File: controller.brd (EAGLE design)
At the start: 46.3 x 36.8 mm, 27 parts, among them U1 10118194-MICRO-USB, U2 LM3671MF-3.3/NOPBMF05A-M, U3 SN74LVC1T45DBVRDBV6-M, U4 SN74LVC1T45DBVRDBV6-M, U5 SS8050-G, U6 SS8050-G

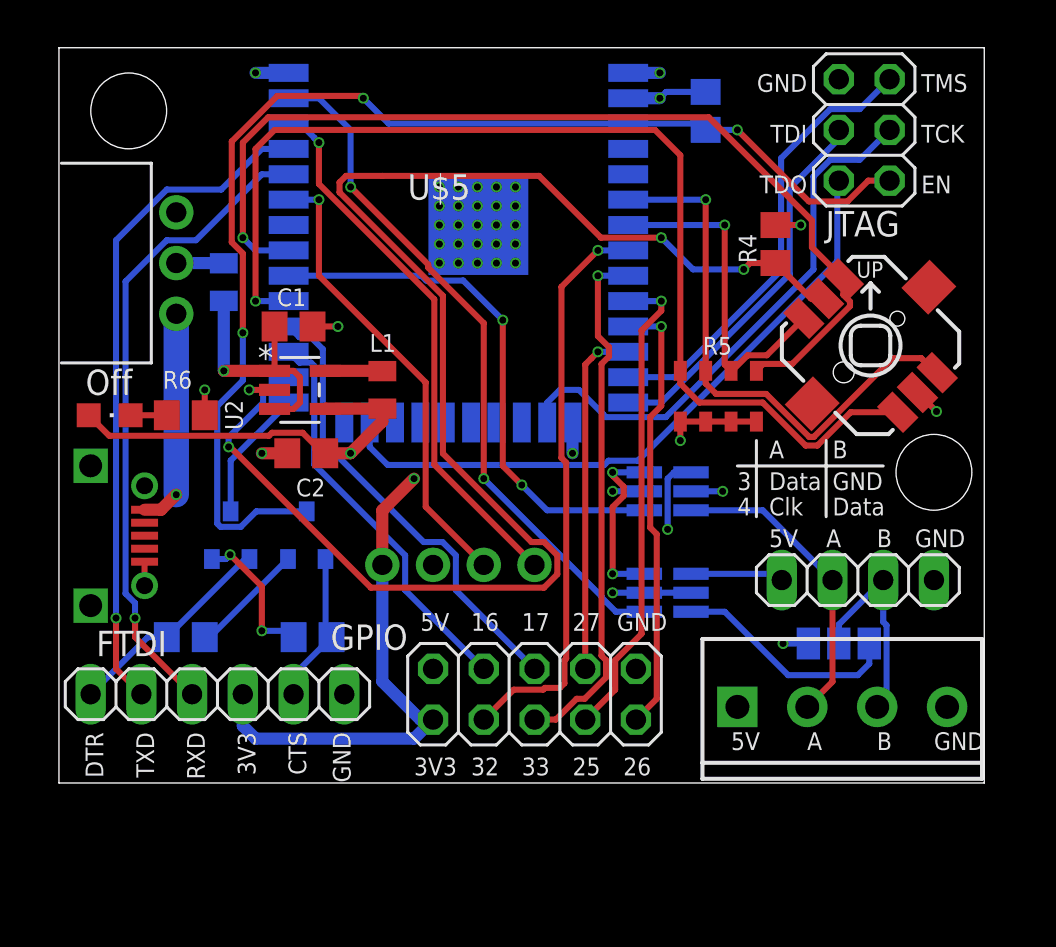
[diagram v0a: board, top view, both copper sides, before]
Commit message: Fixed a bunch of bugs in v1.0
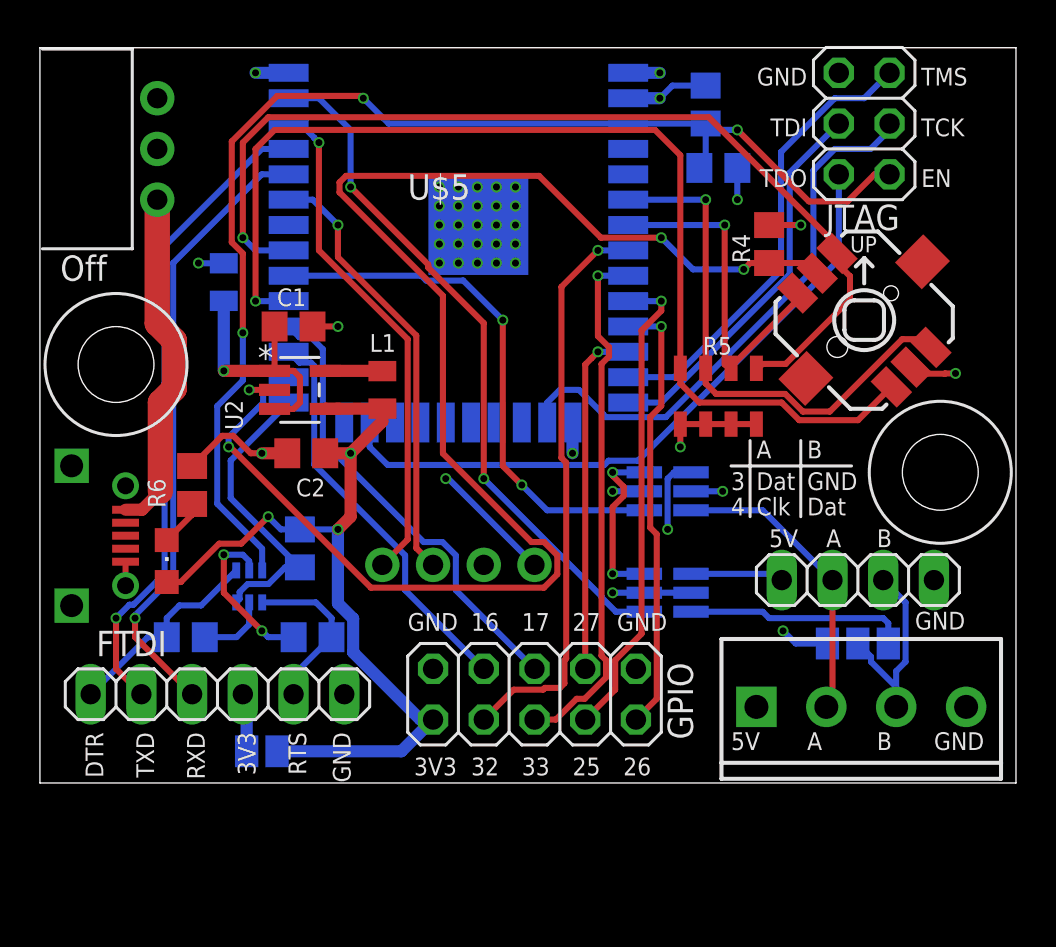
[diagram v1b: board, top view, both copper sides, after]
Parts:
- removed U6: SS8050-G, nebrius:SC-59
- added C3: 0.1uF, rcl:C0805
- added R7: (no value), rcl:R0805
- added SJ2: (no value), jumper:SJ
- R6: value 220 -> 1k
- U5: value SS8050-G -> MBT3904DW1T1; device nebrius:SC-59 -> nebrius:SOT363
- moved LED1 7.84 mm to (84.5, 56.8), turned to 0 degrees
- moved U$3 5.79 mm to (84.0, 77.5)
- moved U5 3.82 mm to (88.6, 55.6), turned to 0 degrees
- moved R6 3.51 mm to (85.7, 60.6), turned to 270 degrees
- moved S1 1.31 mm to (119.4, 68.9)
- moved J1 0.95 mm to (114.0, 49.5)
- moved SJ1 0.95 mm to (119.1, 52.7)
- moved U1 0.95 mm to (79.7, 58.1)
- moved JP3 0.32 mm to (119.4, 78.7)
- moved R3 0.32 mm to (111.4, 79.7)
- moved R4 0.32 mm to (114.6, 72.7)
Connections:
- new net N$11: JP2.3, SJ2.1
- net +5V: no longer JP7.2
- net EN: now also C3.1, U5.6; no longer U5.3
- net GND: now also C3.2, JP7.2, U$5.3; no longer U$5.2
- net IO0: now also R7.1, U5.3; no longer U6.3
- net N$12: now also JP2.2, R2.2, U5.1; no longer JP2.6, R1.2, U6.2
- net N$4: now also U5.2; no longer U5.1
- net N$5: now also U5.5; no longer U6.1
- net N$6: now also JP2.6, R1.2, U5.4; no longer JP2.2, R2.2, U5.2
- net SCL: now also U$5.2; no longer U$5.3
- net SDA: now also U$5.1; no longer U$5.4
- net VCC: now also R7.2, SJ2.2, U$5.4; no longer JP2.3, U$5.1
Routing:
- net IO0: track 6.65 -> 15.0 mm
- net GND: track 21.8 -> 28.8 mm
- net N$2: track 11.0 -> 17.4 mm, vias 1 -> 0
- net N$11: track 0.00 -> 2.94 mm
- net VCC: track 64.5 -> 67.4 mm, vias 7 -> 9
- net N$6: track 7.68 -> 10.4 mm
- net N$12: track 10.8 -> 8.40 mm
- net N$4: track 5.79 -> 3.59 mm
- net SDA: track 27.5 -> 25.4 mm
- net TXD: track 33.8 -> 32.3 mm
- net RXD: track 32.4 -> 31.2 mm
- net SCL: track 23.2 -> 22.0 mm
- net RIGHT: track 27.7 -> 26.6 mm
- net +5V: track 10.9 -> 9.81 mm, vias 1 -> 2
- net N$5: track 7.19 -> 8.19 mm
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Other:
- board size 46.3 x 36.8 mm -> 48.9 x 36.8 mm
- board text added: "Dat"
- board text added: "RTS"
- board text added: "RVL Controller v1.1 Copyright Bryan Hughes October 2019"
- board text removed: "CTS"
- board text removed: "Data"
- board text removed: "RVL Controller v1.0 Copyright Bryan Hughes October 2019"

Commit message: Tweaks and bug fixes from v1.1 board
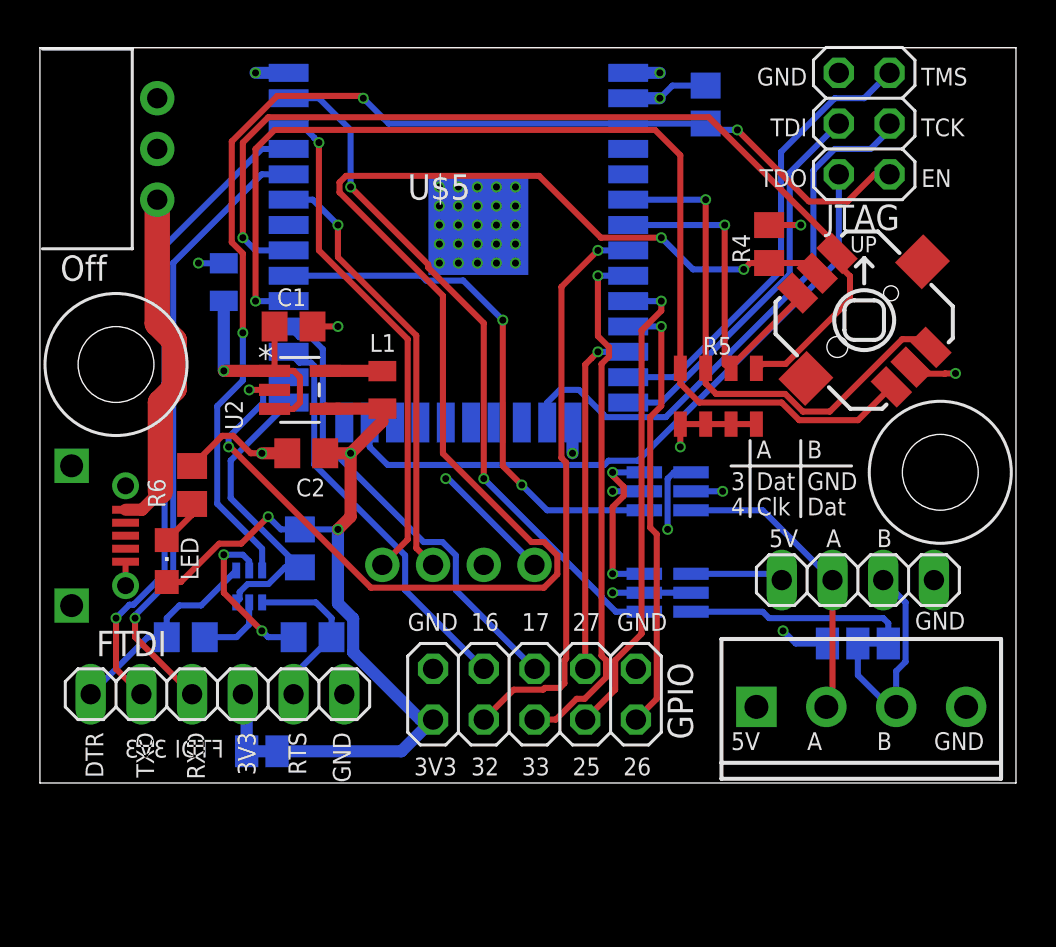
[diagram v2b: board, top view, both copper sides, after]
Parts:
- removed C3: 0.1uF, rcl:C0805
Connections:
- removed net N$11: JP2.3, SJ2.1
- removed net N$8: SJ1.1, U3.3
- net DOWN: now also R5.P$4, S1.A, U$2.31; no longer R5.P$1, S1.D, U$2.29
- net EN: no longer C3.1
- net GND: no longer C3.2
- net N$7: now also SJ1.1, U3.3
- net UP: now also R5.P$1, S1.D, U$2.29; no longer R5.P$4, S1.A, U$2.31
- net VCC: now also JP2.3, SJ2.1
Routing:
- net N$7: track 9.98 -> 23.8 mm
- net N$8: track 11.1 -> 0.00 mm
- net UP: track 49.3 -> 54.9 mm
- net DOWN: track 54.9 -> 49.3 mm
- net VCC: track 67.4 -> 71.8 mm
- net N$11: track 2.94 -> 0.00 mm
- net EN: track 62.2 -> 59.8 mm
- net GND: track 28.8 -> 27.2 mm, vias 37 -> 36
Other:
- board text added: "FTDI 3V3"
- board text added: "LED"
- board text added: "RVL Controller v1.2 Copyright Bryan Hughes October 2019"
- board text removed: "RVL Controller v1.1 Copyright Bryan Hughes October 2019"
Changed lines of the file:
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@@
 <?xml version="1.0" encoding="utf-8"?>
 <!DOCTYPE eagle SYSTEM "eagle.dtd">
-<eagle version="9.5.1">
+<eagle version="9.5.2">
 <drawing>
 <settings>
@@
 <wire x1="112.7125" y1="61.595" x2="118.745" y2="61.595" width="0.1524" layer="21"/>
 <wire x1="116.205" y1="62.865" x2="116.205" y2="59.055" width="0.1524" layer="21"/>
-<text x="124.46" y="69.215" size="0.889" layer="22" font="vector" ratio="20" rot="MR0">RVL Controller v1.1
+<text x="124.46" y="69.215" size="0.889" layer="22" font="vector" ratio="20" rot="MR0">RVL Controller v1.2
 Copyright Bryan Hughes
 October 2019</text>
 <circle x="81.915" y="66.675" radius="3.556" width="0.1524" layer="21"/>
 <circle x="123.19" y="61.2775" radius="3.556" width="0.1524" layer="21"/>
+<text x="86.0425" y="55.88" size="0.889" layer="25" font="vector" ratio="20" rot="R90">LED</text>
+<text x="87.3125" y="46.99" size="0.889" layer="25" font="vector" ratio="20" rot="MR0">FTDI 3V3</text>
 </plain>
 <attributes>
@@
 <attribute name="VALUE" x="89.6825" y="52.8625" size="1.27" layer="28" rot="MR0" display="off"/>
 </element>
-<element name="C3" library="rcl" library_urn="urn:adsk.eagle:library:334" package="C0805" package3d_urn="urn:adsk.eagle:package:23617/2" value="0.1uF" x="112.0775" y="76.5175" smashed="yes" rot="MR180">
-<attribute name="NAME" x="110.8075" y="75.2475" size="0.762" layer="26" font="vector" ratio="20" rot="MR180"/>
-<attribute name="POPULARITY" value="63" x="112.0775" y="76.5175" size="1.778" layer="28" rot="MR180" display="off"/>
-<attribute name="SPICEPREFIX" value="C" x="112.0775" y="76.5175" size="1.778" layer="28" rot="MR180" display="off"/>
-<attribute name="VALUE" x="110.8075" y="79.0575" size="1.27" layer="28" rot="MR180" display="off"/>
-</element>
 <element name="SJ2" library="jumper" library_urn="urn:adsk.eagle:library:252" package="SJ" package3d_urn="urn:adsk.eagle:package:15471/1" value="" x="89.2175" y="47.3075" smashed="yes" rot="MR180">
 <attribute name="NAME" x="87.5665" y="46.1645" size="1.27" layer="26" ratio="10" rot="MR180" display="off"/>
@@
 <via x="89.2175" y="62.23" extent="1-16" drill="0.35"/>
 <contactref element="JP7" pad="2"/>
-<contactref element="C3" pad="2"/>
-<wire x1="113.0275" y1="76.5175" x2="113.0275" y2="74.9325" width="0.3048" layer="16"/>
-<wire x1="113.0275" y1="74.9325" x2="113.03" y2="74.93" width="0.3048" layer="16"/>
-<via x="113.03" y="74.93" extent="1-16" drill="0.35"/>
 <wire x1="89.2175" y1="62.23" x2="88.6592" y2="62.23" width="0.3048" layer="1"/>
 <wire x1="88.6592" y1="62.23" x2="87.7836" y2="63.1056" width="0.3048" layer="1"/>
@@
 <wire x1="89.535" y1="59.055" x2="90.1725" y2="58.4175" width="0.3048" layer="16"/>
 <wire x1="90.1725" y1="58.4175" x2="91.1225" y2="58.4175" width="0.3048" layer="16"/>
+<contactref element="JP2" pad="3"/>
+<contactref element="SJ2" pad="1"/>
+<wire x1="88.265" y1="50.165" x2="88.4555" y2="49.9745" width="0.6096" layer="16"/>
+<wire x1="88.4555" y1="49.9745" x2="88.4555" y2="47.3075" width="0.6096" layer="16"/>
+<wire x1="88.4555" y1="47.3075" x2="89.9795" y2="47.3075" width="0.6096" layer="16"/>
 </signal>
 <signal name="N$2">
@@
 <wire x1="86.9823" y1="59.7027" x2="89.2325" y2="57.4525" width="0.3048" layer="16"/>
 <wire x1="89.2325" y1="57.4525" x2="89.2325" y2="56.3625" width="0.3048" layer="16"/>
-<contactref element="C3" pad="1"/>
 <wire x1="119.9002625" y1="76.2" x2="120.65" y2="76.2" width="0.3048" layer="1"/>
-<wire x1="111.4425" y1="78.7425" x2="111.4425" y2="76.8325" width="0.3048" layer="16"/>
-<wire x1="111.4425" y1="76.8325" x2="111.1275" y2="76.5175" width="0.3048" layer="16"/>
 </signal>
 <signal name="TXD">
@@
 <via x="87.3125" y="57.15" extent="1-16" drill="0.35"/>
 </signal>
-<signal name="N$8">
-<contactref element="U3" pad="3"/>
-<contactref element="SJ1" pad="1"/>
-<wire x1="114.2975" y1="54.295" x2="114.6175" y2="53.975" width="0.3048" layer="16"/>
-<wire x1="114.6175" y1="53.975" x2="120.3325" y2="53.975" width="0.3048" layer="16"/>
-<wire x1="120.3325" y1="53.975" x2="120.5865" y2="53.721" width="0.3048" layer="16"/>
-<wire x1="120.5865" y1="53.721" x2="120.5865" y2="52.705" width="0.3048" layer="16"/>
-<wire x1="110.7059" y1="54.295" x2="114.2975" y2="54.295" width="0.3048" layer="16"/>
-</signal>
 <signal name="N$9">
 <contactref element="U4" pad="3"/>
@@
 <wire x1="117.7925" y1="49.84" x2="117.4825" y2="49.53" width="0.3048" layer="1"/>
 </signal>
-<signal name="UP">
+<signal name="DOWN">
 <contactref element="S1" pad="A"/>
 <contactref element="R5" pad="P$4"/>
@@
 <wire x1="115.448971875" y1="66.7051" x2="114.3301" y2="66.7051" width="0.3048" layer="1"/>
 </signal>
-<signal name="DOWN">
+<signal name="UP">
 <contactref element="S1" pad="D"/>
 <contactref element="R5" pad="P$1"/>
@@
 <contactref element="SJ1" pad="2"/>
 <contactref element="JP1" pad="3"/>
-<wire x1="119.0625" y1="52.705" x2="119.7229" y2="52.0446" width="0.3048" layer="16"/>
-<wire x1="119.7229" y1="52.0446" x2="119.7229" y2="51.78916875" width="0.3048" layer="16"/>
-<wire x1="120.9825" y1="50.52956875" x2="120.9825" y2="49.53" width="0.3048" layer="16"/>
-<wire x1="119.7229" y1="51.78916875" x2="120.9825" y2="50.52956875" width="0.3048" layer="16"/>
-<wire x1="120.9825" y1="51.32156875" x2="120.9825" y2="50.52956875" width="0.3048" layer="16"/>
+<wire x1="120.9825" y1="51.32156875" x2="120.9825" y2="49.53" width="0.3048" layer="16"/>
 <wire x1="121.4501" y1="51.78916875" x2="120.9825" y2="51.32156875" width="0.3048" layer="16"/>
 <wire x1="120.3325" y1="55.88" x2="121.4501" y2="54.7624" width="0.3048" layer="16"/>
 <wire x1="121.4501" y1="54.7624" x2="121.4501" y2="51.78916875" width="0.3048" layer="16"/>
-</signal>
-<signal name="N$11">
-<contactref element="JP2" pad="3"/>
-<contactref element="SJ2" pad="1"/>
-<wire x1="88.265" y1="50.165" x2="88.4555" y2="49.9745" width="0.6096" layer="16"/>
-<wire x1="88.4555" y1="49.9745" x2="88.4555" y2="47.3075" width="0.6096" layer="16"/>
+<contactref element="U3" pad="3"/>
+<contactref element="SJ1" pad="1"/>
+<wire x1="114.2975" y1="54.295" x2="114.6175" y2="53.975" width="0.3048" layer="16"/>
+<wire x1="114.6175" y1="53.975" x2="120.3325" y2="53.975" width="0.3048" layer="16"/>
+<wire x1="120.3325" y1="53.975" x2="120.5865" y2="53.721" width="0.3048" layer="16"/>
+<wire x1="120.5865" y1="53.721" x2="120.5865" y2="52.705" width="0.3048" layer="16"/>
+<wire x1="110.7059" y1="54.295" x2="114.2975" y2="54.295" width="0.3048" layer="16"/>
+<wire x1="119.0625" y1="52.705" x2="119.0625" y2="51.1175" width="0.3048" layer="16"/>
+<wire x1="119.0625" y1="51.1175" x2="120.65" y2="49.53" width="0.3048" layer="16"/>
+<wire x1="120.65" y1="49.53" x2="120.9825" y2="49.53" width="0.3048" layer="16"/>
+<wire x1="119.0625" y1="52.705" x2="120.5865" y2="52.705" width="0.3048" layer="16"/>
 </signal>
 </signals>

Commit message: Made a lot of progress with redesign
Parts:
- removed F1: FUSE-0805, nebrius:R0805
- removed JP3: JTAG, pinhead:2X03
- removed JP7: GPIO, pinhead:2X05
- removed R1, R2: 10k, rcl:R0805
- removed U$3: CL-SA-12C4, nebrius:CL-SA-12C4
- removed U5: MBT3904DW1T1, nebrius:SOT363
- added S2, S3: (no value), SparkFun-Switches:TACTILE_SWITCH_SMD_4.6X2.8MM
- JP2: value FTDI -> (none); device pinhead:1X06 -> pinhead:2X08
- R7: value (none) -> 10k
- moved JP2 12.1 mm to (99.1, 49.8), turned to 0 degrees
- moved SJ2 9.34 mm to (83.8, 54.9), turned to 0 degrees
- moved R6 5.72 mm to (87.6, 55.2)
- moved U1 4.76 mm to (82.5, 61.9)
- moved J1 2.22 mm to (111.8, 49.5)
- moved LED1 1.85 mm to (83.5, 55.2), turned to 270 degrees
- moved SJ1 1.59 mm to (117.5, 52.7)
- moved JP1 0.64 mm to (118.4, 55.9)
- moved S1 0.45 mm to (119.1, 68.6)
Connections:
- removed net N$12: JP2.2, R2.2, U5.1
- removed net N$4: R1.1, U5.2
- removed net N$5: R2.1, U5.5
- removed net N$6: JP2.6, R1.2, U5.4
- net +5V: no longer F1.1, U$3.2
- net EN: now also JP2.11, S3.3, S3.4; no longer JP3.1, U5.6
- net GND: now also S2.3, S2.4, S3.1, S3.2; no longer JP2.1, JP3.6, JP7.10, JP7.2
- net GPIO16: now also JP2.4; no longer JP7.4
- net GPIO17: now also JP2.6; no longer JP7.6
- net GPIO25: now also JP2.7; no longer JP7.7
- net GPIO26: now also JP2.9; no longer JP7.9
- net GPIO27: now also JP2.8; no longer JP7.8
- net GPIO32: now also JP2.3; no longer JP7.3
- net GPIO33: now also JP2.5; no longer JP7.5
- net IO0: now also S2.1, S2.2; no longer U5.3
- net N$2: now also JP2.2; no longer U$3.3, U1.1
- net N$3: now also U1.1; no longer F1.2
- net RXD: now also JP2.12; no longer JP2.4
- net TCK: now also JP2.13; no longer JP3.3
- net TDI: now also JP2.16; no longer JP3.4
- net TDO: now also JP2.14; no longer JP3.2
- net TMS: now also JP2.15; no longer JP3.5
- net TXD: now also JP2.10; no longer JP2.5
- net VCC: now also JP2.1; no longer JP2.3, JP7.1
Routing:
- net VCC: track 71.8 -> 32.5 mm, vias 9 -> 7
- net EN: track 59.8 -> 27.0 mm, vias 3 -> 2
- net TXD: track 32.3 -> 0.00 mm, vias 1 -> 0
- net RXD: track 31.2 -> 0.00 mm, vias 1 -> 0
- net TCK: track 28.2 -> 0.00 mm
- net GPIO33: track 26.6 -> 0.00 mm, vias 1 -> 0
- net GPIO25: track 24.2 -> 0.00 mm, vias 1 -> 0
- net TMS: track 22.9 -> 0.00 mm
- net N$7: track 23.8 -> 1.52 mm
- net GPIO26: track 22.1 -> 0.00 mm, vias 1 -> 0
- net TDI: track 19.3 -> 0.00 mm
- net TDO: track 33.6 -> 15.1 mm
- net GPIO27: track 17.7 -> 0.00 mm, vias 1 -> 0
- net N$2: track 17.4 -> 0.00 mm
- net DOWN: track 49.3 -> 32.1 mm
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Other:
- board size 48.9 x 36.8 mm -> 42.8 x 36.8 mm
- board text added: "Boot"
- board text added: "Rst"
- board text removed: "FTDI 3V3"
- board text removed: "Off"
